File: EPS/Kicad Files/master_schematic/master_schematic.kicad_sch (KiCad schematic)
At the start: 0 parts

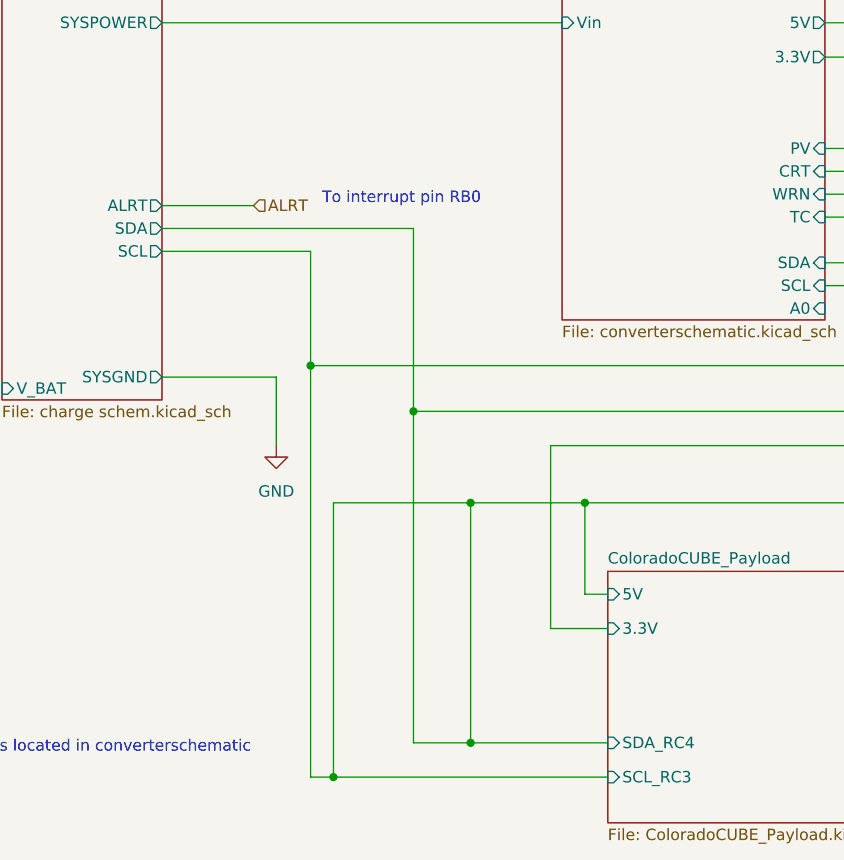
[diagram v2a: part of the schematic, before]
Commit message: all traces routed (EPS)
all nets, traces, etc connected.....now we need to run DRC...errors are inevitable
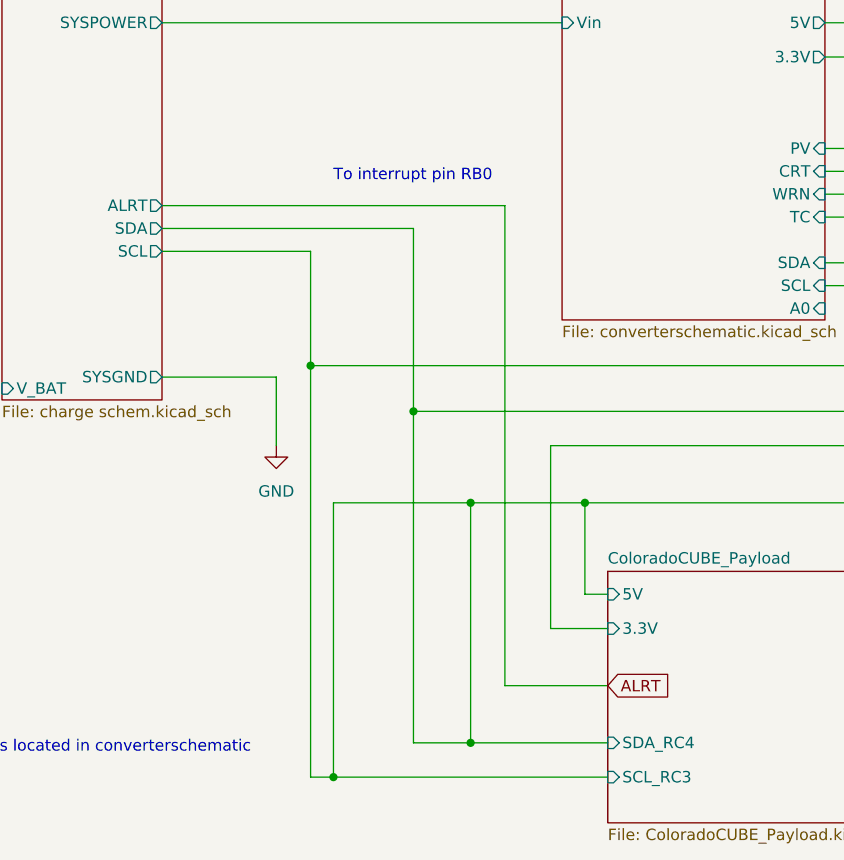
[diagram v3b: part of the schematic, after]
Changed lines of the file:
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@@
     (stroke (width 0) (type default) (color 0 0 0 0))
   )
-  (wire (pts (xy 77.47 87.63) (xy 87.63 87.63))
+  (wire (pts (xy 77.47 87.63) (xy 115.57 87.63))
     (stroke (width 0) (type default) (color 0 0 0 0))
   )
@@
   )
   (wire (pts (xy 151.13 93.98) (xy 160.02 93.98))
+    (stroke (width 0) (type default) (color 0 0 0 0))
+  )
+  (wire (pts (xy 115.57 140.97) (xy 127 140.97))
     (stroke (width 0) (type default) (color 0 0 0 0))
   )
@@
     (stroke (width 0) (type default) (color 0 0 0 0))
   )
+  (wire (pts (xy 115.57 87.63) (xy 115.57 140.97))
+    (stroke (width 0) (type default) (color 0 0 0 0))
+  )
   (wire (pts (xy 172.72 67.31) (xy 186.69 67.31))
     (stroke (width 0) (type default) (color 0 0 0 0))
@@
     (effects (font (size 1.27 1.27)) (justify left bottom))
   )
-  (text "To interrupt pin RB0" (at 95.25 87.63 0)
+  (text "To interrupt pin RB0" (at 96.52 85.09 0)
     (effects (font (size 1.27 1.27)) (justify left bottom))
   )
-  (hierarchical_label "ALRT" (shape input) (at 87.63 87.63 0)
+  (global_label "ALRT" (shape input) (at 127 140.97 0) (fields_autoplaced)
     (effects (font (size 1.27 1.27)) (justify left))
+    (property "Intersheet References" "${INTERSHEET_REFS}" (id 0) (at 133.7674 140.8906 0)
+      (effects (font (size 1.27 1.27)) (justify left) hide)
+    )
   )
   (symbol (lib_id "power:GND") (at 90.17 114.3 0) (unit 1)

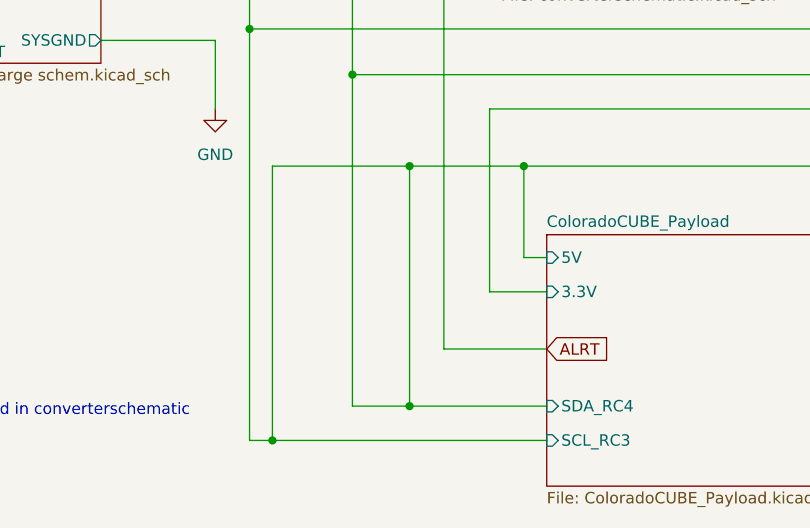
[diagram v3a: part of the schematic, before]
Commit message: eps pcb update
all errors and warnings corrected
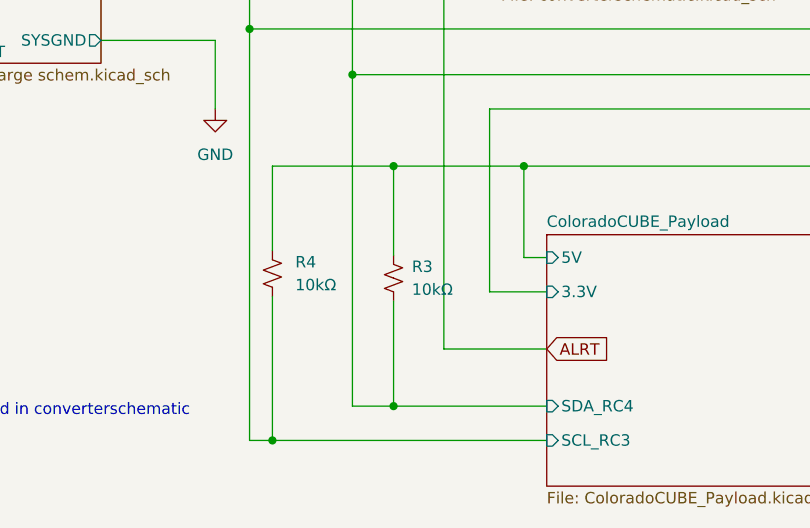
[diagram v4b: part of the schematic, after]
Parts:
- added R3, R4: 10kΩ, Resistor_SMD:R_0603_1608Metric, symbol Device:R_Small_US
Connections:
- net ColoradoCUBE_Payload/5V: now also R3.1, R4.1
- new net ColoradoCUBE_Payload/SCL_RC3: R4.2
- new net ColoradoCUBE_Payload/SDA_RC4: R3.2
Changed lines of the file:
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@@
     (company "MSU Denver Senior Project")
   )
+  (junction (at 109.982 120.65) (diameter 0) (color 0 0 0 0)
+  )
   (junction (at 105.41 110.49) (diameter 0) (color 0 0 0 0)
   )
   (junction (at 124.46 120.65) (diameter 0) (color 0 0 0 0)
   )
-  (junction (at 111.76 147.32) (diameter 0) (color 0 0 0 0)
+  (junction (at 109.982 147.32) (diameter 0) (color 0 0 0 0)
   )
   (junction (at 93.98 105.41) (diameter 0) (color 0 0 0 0)
-  )
-  (junction (at 111.76 120.65) (diameter 0) (color 0 0 0 0)
   )
   (junction (at 96.52 151.13) (diameter 0) (color 0 0 0 0)
@@
     (stroke (width 0) (type default) (color 0 0 0 0))
   )
+  (wire (pts (xy 96.52 135.128) (xy 96.52 151.13))
+    (stroke (width 0) (type default) (color 0 0 0 0))
+  )
   (wire (pts (xy 157.48 105.41) (xy 93.98 105.41))
     (stroke (width 0) (type default) (color 0 0 0 0))
@@
     (stroke (width 0) (type default) (color 0 0 0 0))
   )
-  (wire (pts (xy 96.52 120.65) (xy 96.52 151.13))
-    (stroke (width 0) (type default) (color 0 0 0 0))
-  )
   (wire (pts (xy 127 134.62) (xy 120.65 134.62))
     (stroke (width 0) (type default) (color 0 0 0 0))
@@
     (stroke (width 0) (type default) (color 0 0 0 0))
   )
+  (wire (pts (xy 96.52 130.048) (xy 96.52 120.65))
+    (stroke (width 0) (type default) (color 0 0 0 0))
+  )
   (wire (pts (xy 246.38 95.25) (xy 246.38 101.6))
     (stroke (width 0) (type default) (color 0 0 0 0))
@@
     (stroke (width 0) (type default) (color 0 0 0 0))
   )
-  (wire (pts (xy 96.52 120.65) (xy 111.76 120.65))
-    (stroke (width 0) (type default) (color 0 0 0 0))
-  )
-  (wire (pts (xy 111.76 147.32) (xy 127 147.32))
-    (stroke (width 0) (type default) (color 0 0 0 0))
-  )
-  (wire (pts (xy 105.41 147.32) (xy 111.76 147.32))
+  (wire (pts (xy 96.52 151.13) (xy 127 151.13))
+    (stroke (width 0) (type default) (color 0 0 0 0))
+  )
+  (wire (pts (xy 105.41 147.32) (xy 109.982 147.32))
     (stroke (width 0) (type default) (color 0 0 0 0))
   )
@@
     (stroke (width 0) (type default) (color 0 0 0 0))
   )
+  (wire (pts (xy 109.982 135.636) (xy 109.982 147.32))
+    (stroke (width 0) (type default) (color 0 0 0 0))
+  )
   (wire (pts (xy 93.98 105.41) (xy 93.98 151.13))
     (stroke (width 0) (type default) (color 0 0 0 0))
@@
     (stroke (width 0) (type default) (color 0 0 0 0))
   )
-  (wire (pts (xy 96.52 151.13) (xy 127 151.13))
+  (wire (pts (xy 109.982 147.32) (xy 127 147.32))
     (stroke (width 0) (type default) (color 0 0 0 0))
   )
@@
     (stroke (width 0) (type default) (color 0 0 0 0))
   )
-  (wire (pts (xy 111.76 120.65) (xy 124.46 120.65))
+  (wire (pts (xy 96.52 120.65) (xy 109.982 120.65))
     (stroke (width 0) (type default) (color 0 0 0 0))
   )
@@
     (stroke (width 0) (type default) (color 0 0 0 0))
   )
+  (wire (pts (xy 109.982 120.65) (xy 124.46 120.65))
+    (stroke (width 0) (type default) (color 0 0 0 0))
+  )
   (wire (pts (xy 198.12 67.31) (xy 210.82 67.31))
     (stroke (width 0) (type default) (color 0 0 0 0))
   )
-  (wire (pts (xy 111.76 120.65) (xy 111.76 147.32))
+  (wire (pts (xy 109.982 130.556) (xy 109.982 120.65))
     (stroke (width 0) (type default) (color 0 0 0 0))
   )
@@
     )
     (pin "1")
+  )
+  (symbol (lib_id "Device:R_Small_US") (at 96.52 132.588 0) (unit 1)
+    (in_bom yes) (on_board yes) (fields_autoplaced)
+    (property "Reference" "R4" (id 0) (at 99.06 131.3179 0)
+      (effects (font (size 1.27 1.27)) (justify left))
+    )
+    (property "Value" "10kΩ" (id 1) (at 99.06 133.8579 0)
+      (effects (font (size 1.27 1.27)) (justify left))
+    )
+    (property "Footprint" "Resistor_SMD:R_0603_1608Metric" (id 2) (at 96.52 132.588 0)
+      (effects (font (size 1.27 1.27)) hide)
+    )
+    (property "Datasheet" "~" (id 3) (at 96.52 132.588 0)
+      (effects (font (size 1.27 1.27)) hide)
+    )
+    (pin "1")
+    (pin "2")
+  )
+  (symbol (lib_id "Device:R_Small_US") (at 109.982 133.096 0) (unit 1)
+    (in_bom yes) (on_board yes) (fields_autoplaced)
+    (property "Reference" "R3" (id 0) (at 112.014 131.8259 0)
+      (effects (font (size 1.27 1.27)) (justify left))
+    )
+    (property "Value" "10kΩ" (id 1) (at 112.014 134.3659 0)
+      (effects (font (size 1.27 1.27)) (justify left))
+    )
+    (property "Footprint" "Resistor_SMD:R_0603_1608Metric" (id 2) (at 109.982 133.096 0)
+      (effects (font (size 1.27 1.27)) hide)
+    )
+    (property "Datasheet" "~" (id 3) (at 109.982 133.096 0)
+      (effects (font (size 1.27 1.27)) hide)
+    )
+    (pin "1")
+    (pin "2")
   )
   (sheet (at 210.82 50.8) (size 25.4 68.58) (fields_autoplaced)
@@
     (path "/26a06af6-a463-4c0b-bc99-b7ef2964e4cd" (page "3"))
     (path "/009ce997-1584-43ca-93af-c5bcacd4d4e9" (page "5"))
-    (path "/3a06e4e0-634b-426a-a0ab-d37016f35ddc/a47b42ae-0735-4637-85df-404ec278273a" (page "#"))
     (path "/3a06e4e0-634b-426a-a0ab-d37016f35ddc" (page "6"))
     (path "/68881549-1588-438c-abf8-f6f2c2b6b5a2" (page "8"))
     (path "/3a06e4e0-634b-426a-a0ab-d37016f35ddc/4e16fedc-a38b-401e-a5de-03896de0e471" (page "#"))
+    (path "/3a06e4e0-634b-426a-a0ab-d37016f35ddc/a47b42ae-0735-4637-85df-404ec278273a" (page "#"))
   )
   (symbol_instances
@@
       (reference "C21") (unit 1) (value "0.1uF") (footprint "Capacitor_SMD:C_0603_1608Metric")
     )
-    (path "/68881549-1588-438c-abf8-f6f2c2b6b5a2/4c8bce28-a190-4be2-ac35-9540cf27f8ae"
-      (reference "CR1") (unit 1) (value "BZX884B5V1L-HG3-08") (footprint "hg3-08:BZX884B5V1L-HG3-08")
-    )
     (path "/26a06af6-a463-4c0b-bc99-b7ef2964e4cd/68ee057d-8a81-4aa4-8890-50b1d294969a"
       (reference "D1") (unit 1) (value "LED") (footprint "LED_SMD:LED_0603_1608Metric")
@@
       (reference "D3") (unit 1) (value "DIODE") (footprint "Diode_SMD:D_0805_2012Metric")
     )
+    (path "/68881549-1588-438c-abf8-f6f2c2b6b5a2/4c8bce28-a190-4be2-ac35-9540cf27f8ae"
+      (reference "D3") (unit 1) (value "BZX884B5V1L-HG3-08") (footprint "hg3-08:BZX884B5V1L-HG3-08")
+    )
     (path "/68881549-1588-438c-abf8-f6f2c2b6b5a2/be4e4217-76b2-49d6-ac01-d4e643194de5"
       (reference "D4") (unit 1) (value "PD3Z284C3V6-7") (footprint "PD3z284:PD3Z284C3V6-7")
@@
       (reference "R2") (unit 1) (value "PSF4NTEBL500F") (footprint "psf4nt:PSF4NTEBL500F")
     )
+    (path "/f9d52ea2-de3d-4b16-a251-d5e42189425d"
+      (reference "R3") (unit 1) (value "10kΩ") (footprint "Resistor_SMD:R_0603_1608Metric")
+    )
     (path "/59a4dc33-016c-4cea-b648-6fe1c8836f68/fd96f853-b86f-4839-b405-9056fd204602"
       (reference "R3") (unit 1) (value "10kΩ") (footprint "Resistor_SMD:R_0603_1608Metric")
@@
       (reference "R4") (unit 1) (value "10kΩ") (footprint "Resistor_SMD:R_0603_1608Metric")
     )
+    (path "/b785b49e-0b3f-4721-8858-42bc6802f4dd"
+      (reference "R4") (unit 1) (value "10kΩ") (footprint "Resistor_SMD:R_0603_1608Metric")
+    )

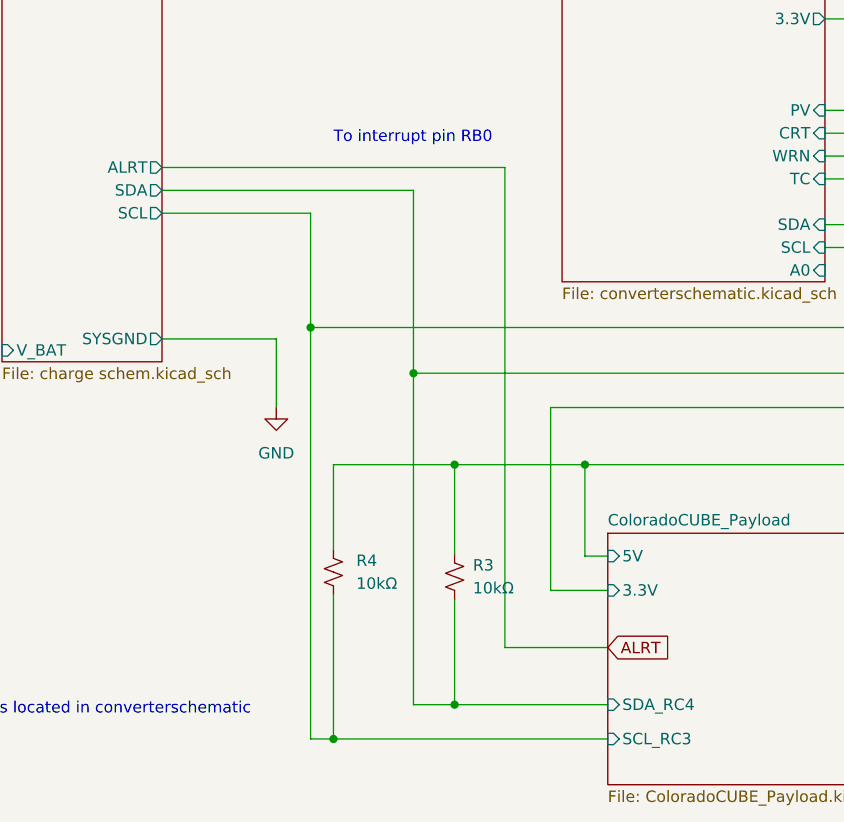
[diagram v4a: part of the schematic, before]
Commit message: Eps board update
vias fixed for manufacturers standards, eliminated ALRT pin on battery gauge
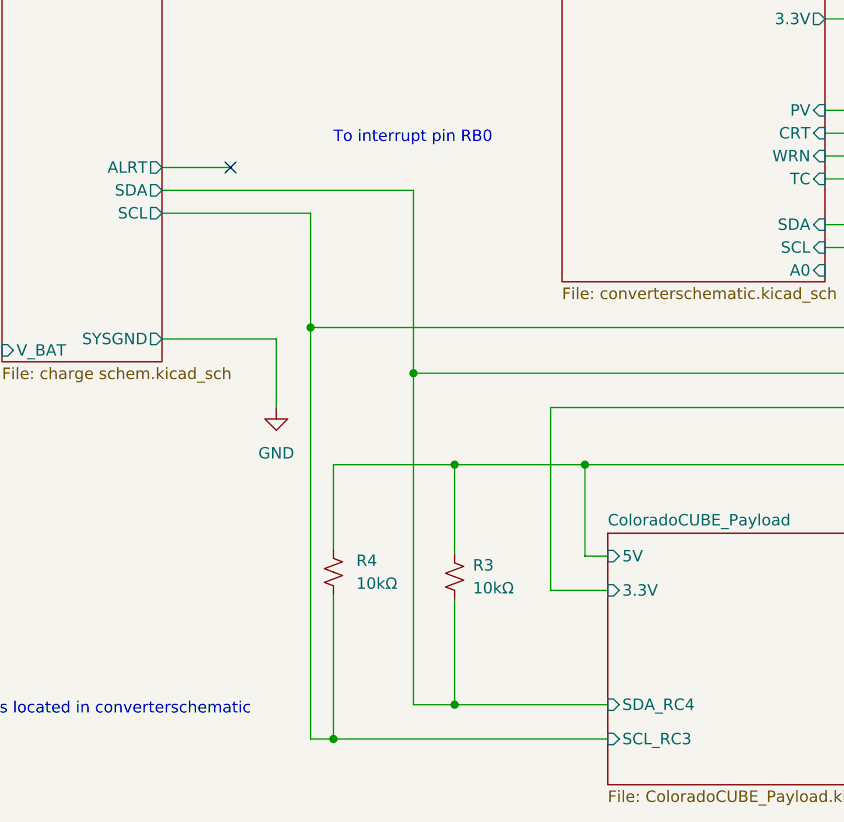
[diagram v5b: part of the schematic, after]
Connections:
- no-connect marks 8 -> 9
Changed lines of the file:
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@@
   (junction (at 198.12 67.31) (diameter 0) (color 0 0 0 0)
   )
+  (no_connect (at 85.09 87.63))
   (no_connect (at 156.21 81.28))
   (no_connect (at 156.21 83.82))
@@
     (stroke (width 0) (type default) (color 0 0 0 0))
   )
+  (wire (pts (xy 77.47 87.63) (xy 85.09 87.63))
+    (stroke (width 0) (type default) (color 0 0 0 0))
+  )
   (wire (pts (xy 172.72 71.12) (xy 175.26 71.12))
     (stroke (width 0) (type default) (color 0 0 0 0))
@@
     (stroke (width 0) (type default) (color 0 0 0 0))
   )
-  (wire (pts (xy 77.47 87.63) (xy 115.57 87.63))
-    (stroke (width 0) (type default) (color 0 0 0 0))
-  )
   (wire (pts (xy 157.48 96.52) (xy 157.48 105.41))
     (stroke (width 0) (type default) (color 0 0 0 0))
@@
     (stroke (width 0) (type default) (color 0 0 0 0))
   )
-  (wire (pts (xy 115.57 140.97) (xy 127 140.97))
-    (stroke (width 0) (type default) (color 0 0 0 0))
-  )
   (wire (pts (xy 177.8 134.62) (xy 201.93 134.62))
     (stroke (width 0) (type default) (color 0 0 0 0))
@@
   )
   (wire (pts (xy 236.22 77.47) (xy 237.49 77.47))
-    (stroke (width 0) (type default) (color 0 0 0 0))
-  )
-  (wire (pts (xy 115.57 87.63) (xy 115.57 140.97))
     (stroke (width 0) (type default) (color 0 0 0 0))
   )
@@
   (text "To interrupt pin RB0" (at 96.52 85.09 0)
     (effects (font (size 1.27 1.27)) (justify left bottom))
-  )
-  (global_label "ALRT" (shape input) (at 127 140.97 0) (fields_autoplaced)
-    (effects (font (size 1.27 1.27)) (justify left))
-    (property "Intersheet References" "${INTERSHEET_REFS}" (id 0) (at 133.7674 140.8906 0)
-      (effects (font (size 1.27 1.27)) (justify left) hide)
-    )
   )
   (symbol (lib_id "power:GND") (at 90.17 114.3 0) (unit 1)
@@
       (reference "D2") (unit 1) (value "LED") (footprint "LED_SMD:LED_0603_1608Metric")
     )
-    (path "/3a06e4e0-634b-426a-a0ab-d37016f35ddc/4bff1f15-0047-457d-ac78-28e14a16e610"
-      (reference "D3") (unit 1) (value "DIODE") (footprint "Diode_SMD:D_0805_2012Metric")
-    )
     (path "/68881549-1588-438c-abf8-f6f2c2b6b5a2/4c8bce28-a190-4be2-ac35-9540cf27f8ae"
       (reference "D3") (unit 1) (value "BZX884B5V1L-HG3-08") (footprint "hg3-08:BZX884B5V1L-HG3-08")
@@
       (reference "D9") (unit 1) (value "YELLOW") (footprint "LED_SMD:LED_0603_1608Metric")
     )
+    (path "/3a06e4e0-634b-426a-a0ab-d37016f35ddc/4bff1f15-0047-457d-ac78-28e14a16e610"
+      (reference "Din1") (unit 1) (value "DIODE") (footprint "Diode_SMD:D_0805_2012Metric")
+    )
     (path "/26a06af6-a463-4c0b-bc99-b7ef2964e4cd/cdbbd672-c242-4d10-880b-b6584a59ec22"
       (reference "J1") (unit 1) (value "USB_C_Receptacle") (footprint "Connector_USB:USB_C_Receptacle_Amphenol_12401610E4-2A")
@@
       (reference "R3") (unit 1) (value "10kΩ") (footprint "Resistor_SMD:R_0603_1608Metric")
     )
-    (path "/59a4dc33-016c-4cea-b648-6fe1c8836f68/fd96f853-b86f-4839-b405-9056fd204602"
-      (reference "R3") (unit 1) (value "10kΩ") (footprint "Resistor_SMD:R_0603_1608Metric")
-    )
-    (path "/59a4dc33-016c-4cea-b648-6fe1c8836f68/7aa48356-0363-4881-a22e-060e5a1f9201"
-      (reference "R4") (unit 1) (value "10kΩ") (footprint "Resistor_SMD:R_0603_1608Metric")
-    )
     (path "/b785b49e-0b3f-4721-8858-42bc6802f4dd"

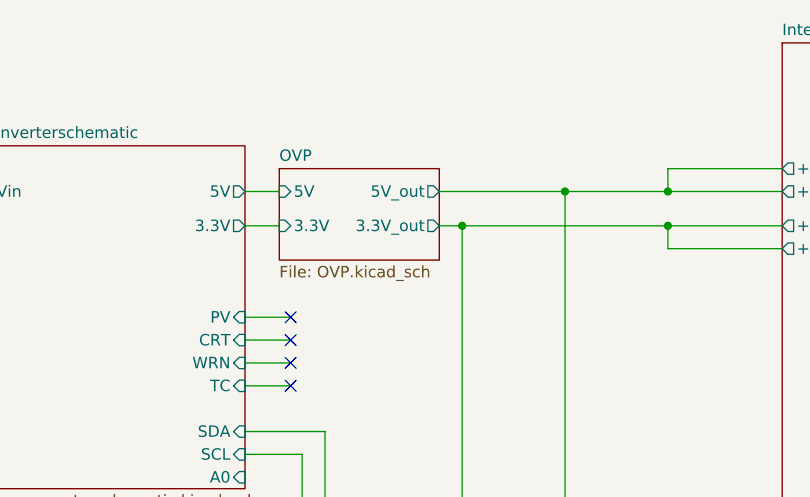
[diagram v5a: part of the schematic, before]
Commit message: eps redesign
updated boost converter
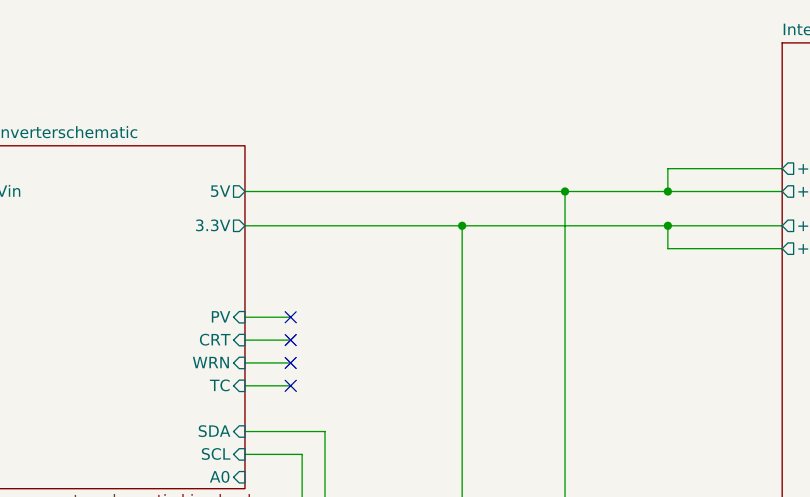
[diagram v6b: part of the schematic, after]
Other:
- removed sheet OVP
